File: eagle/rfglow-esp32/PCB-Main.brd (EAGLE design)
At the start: 20.1 x 75.9 mm, 27 parts, among them IC1 TLC59116PW, J1 4P-SMD-2.0-90D, J2 2P-2.0-90D-SMD, SW1 MK-12C02 G1.5, SW2 DHT-4235A, U1 XC6206P332MR-G-SOT23, U2 Value, X1 87438-06

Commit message: Consolidate libraries, swap regulator
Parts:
- removed C1: 100nf, Seeed-Capacitor:C0402
- ANT1: device Seeed-Connector:U-FL3P-SMD-2.6X2.6X1.0MM -> OPL_Connector:U-FL3P-SMD-2.6X2.6X1.0MM
- C2, C3: device Seeed-Capacitor:C0402 -> OPL_Capacitor:C0402
- J1: device Seeed-Connector:HW4-SMD-2.0-90D -> OPL_Connector:HW4-SMD-2.0-90D
- J2: device Seeed-Connector:HW2-SMD-2.0-90D -> OPL_Connector:HW2-SMD-2.0-90D
- R5, R6, R7: device Seeed-Resistor:R0402 -> OPL_Resistor:R0402
- R8, R9: value 10M 1/16W -> 1M; device Seeed-Resistor:R0402 -> OPL_Resistor:R0402
- SW1: device Seeed-Switch:SW7-SMD-L6.7X2.7X3.2MM -> OPL_Switch:SW7-SMD-L6.7X2.7X3.2MM
- SW2: device Seeed-Switch:SW4-SMD-4.2X3.2X2.5MM -> OPL_Switch:SW4-SMD-4.2X3.2X2.5MM
- U1: value XC6206P332MR-G-SOT23 -> AP2112K-3.3TRG1; device Seeed-IC:SOT-23 -> rfglow-esp32:SOT95P285X140-5N
- U2: device Webench-Regulator:DRC0010J -> Components:DRC0010J
- moved U1 71.2 mm to (-59.1, -16.6)
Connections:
- net GND: now also U1.2; no longer C1.1, U1.1
- net N$17: no longer C1.2
- net V3.3: now also U1.5; no longer U1.2
- net V4.2: now also U1.1

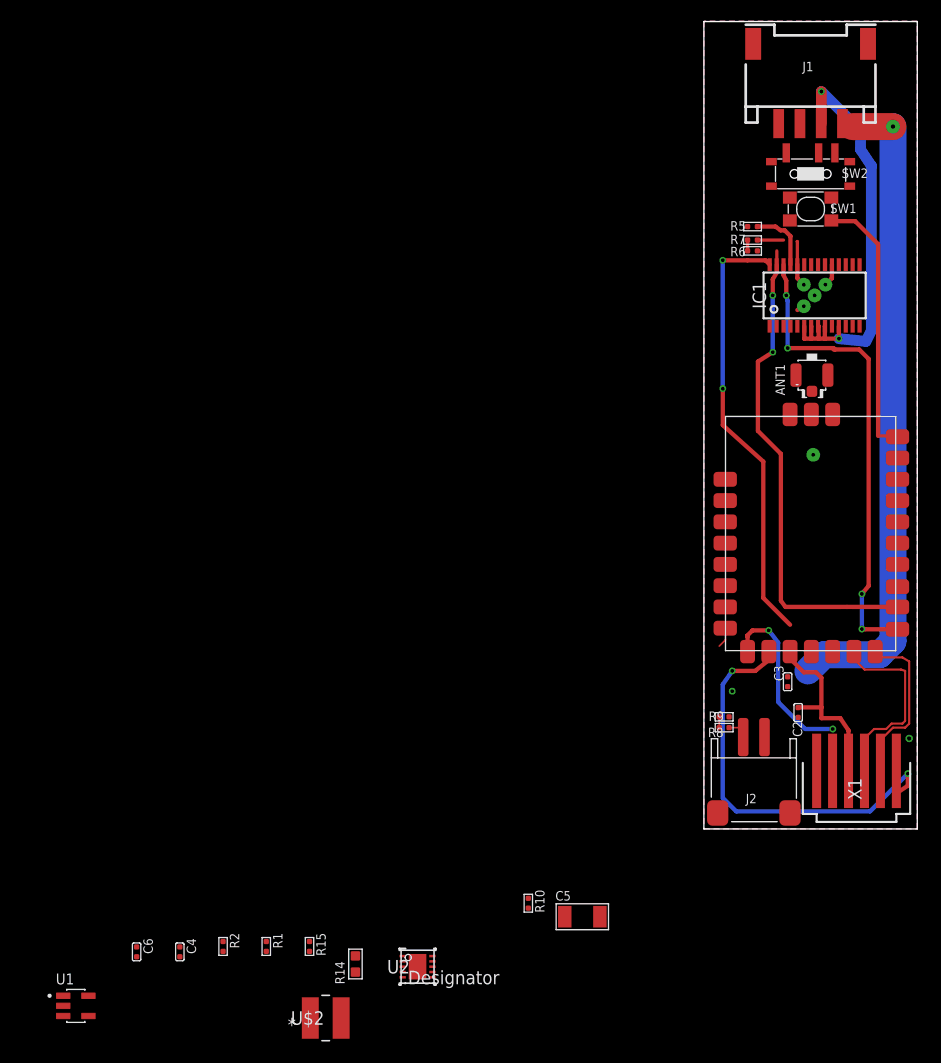
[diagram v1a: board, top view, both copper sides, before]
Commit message: Removed unused parts for esp32, begin integrating actual module
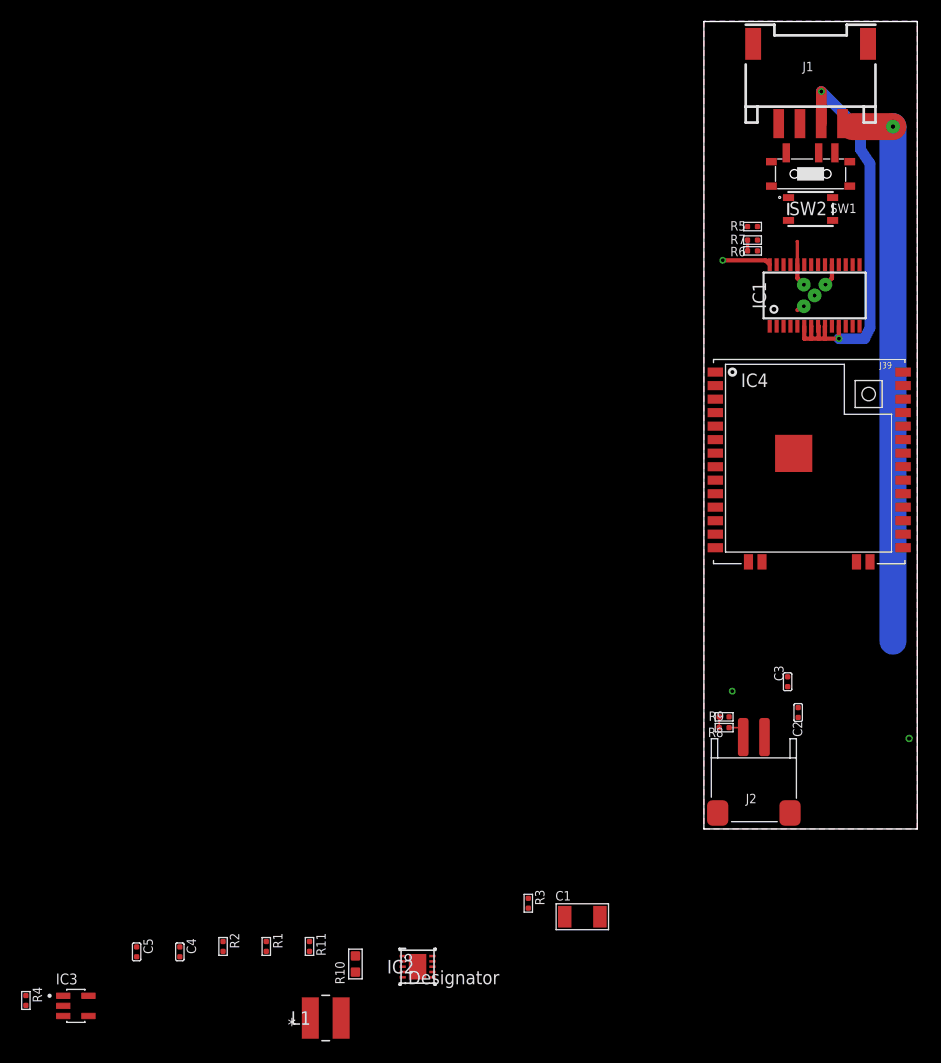
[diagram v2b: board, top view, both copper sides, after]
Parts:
- removed ANT1: U-FL, OPL_Connector:U-FL3P-SMD-2.6X2.6X1.0MM
- removed C6: 10uf, OPL_Capacitor:C0402
- removed R14: 56R, OPL_Resistor:R0603
- removed U$1: PANSTAMP-AVR-2, Components:SMD-PAD-34
- removed X1: 87438-06, Components:87438-06
- added C1: 100uf, OPL_Capacitor:C1206
- added IC4: ESP32-WROOM-32UNOSD, rfglow-esp32:XCVR_ESP32-WROOM-32U
- added R3: 1M, OPL_Resistor:R0402
- added R4: 100K, OPL_Resistor:R0402
- C5: value 100uf -> 10uf; device OPL_Capacitor:C1206 -> OPL_Capacitor:C0402
- R10: value 1M -> 56R; device OPL_Resistor:R0402 -> OPL_Resistor:R0603
- SW2: value DHT-4235A -> SKRPABE010; device OPL_Switch:SW4-SMD-4.2X3.2X2.5MM -> rfglow-esp32:SMT(4.2X3.2)
- moved C5 42.0 mm to (-53.3, -11.6)
- moved R10 17.2 mm to (-32.8, -12.7)
- renumbered R15 to R11, U$2 to L1, U1 to IC3, U2 to IC2
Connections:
- removed net ANT: ANT1.D, U$1.P$31
- removed net AREF: U$1.P$11, X1.2
- removed net N$17: R8.1, R9.2, U$1.P$10
- removed net RST: U$1.P$12, X1.6
- removed net RXD: U$1.P$17, X1.5
- removed net TXD: U$1.P$16, X1.4
- new net 3V3: IC4.2
- new net BATSENSE: R8.1, R9.2
- new net EXP: IC4.39
- new net N$4: IC3.3, R4.1
- net BUTTON: no longer U$1.P$27
- net GND: now also C1.1, IC4.1, IC4.15, IC4.38, R10.1; no longer ANT1.GND1, ANT1.GND2, C6.1, R14.1, U$1.P$14, U$1.P$30, U$1.P$32, X1.1
- net I2CSCL: no longer U$1.P$18
- net I2CSDA: no longer U$1.P$19
- net N$3: now also R3.1; no longer R10.1
- net N$5: now also R10.2; no longer R14.2
- net V3.3: no longer U$1.P$13, X1.3
- net V4.2: now also C1.2, R3.2, R4.2; no longer C5.2, IC3.3, R10.2
- net VBAT: now also C5.2; no longer C6.2
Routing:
- net V3.3: track 61.9 -> 5.59 mm, vias 2 -> 1
- net I2CSCL: track 47.5 -> 0.00 mm, vias 4 -> 0
- net I2CSDA: track 46.3 -> 0.00 mm, vias 2 -> 0
- net RST: track 42.0 -> 0.00 mm, vias 2 -> 0
- net BUTTON: track 25.2 -> 0.10 mm
- net RXD: track 19.6 -> 0.00 mm
- net AREF: track 17.0 -> 0.00 mm, vias 2 -> 0
- net TXD: track 15.6 -> 0.00 mm
- net V4.2: track 62.4 -> 53.3 mm
- net N$7: track 6.12 -> 0.00 mm
- net N$17: track 2.96 -> 0.00 mm
- net BATSENSE: track 0.00 -> 1.02 mm
- net GND: vias 7 -> 6

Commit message: Board layout with UART but without LIPO charger, submitted this one to PCBA
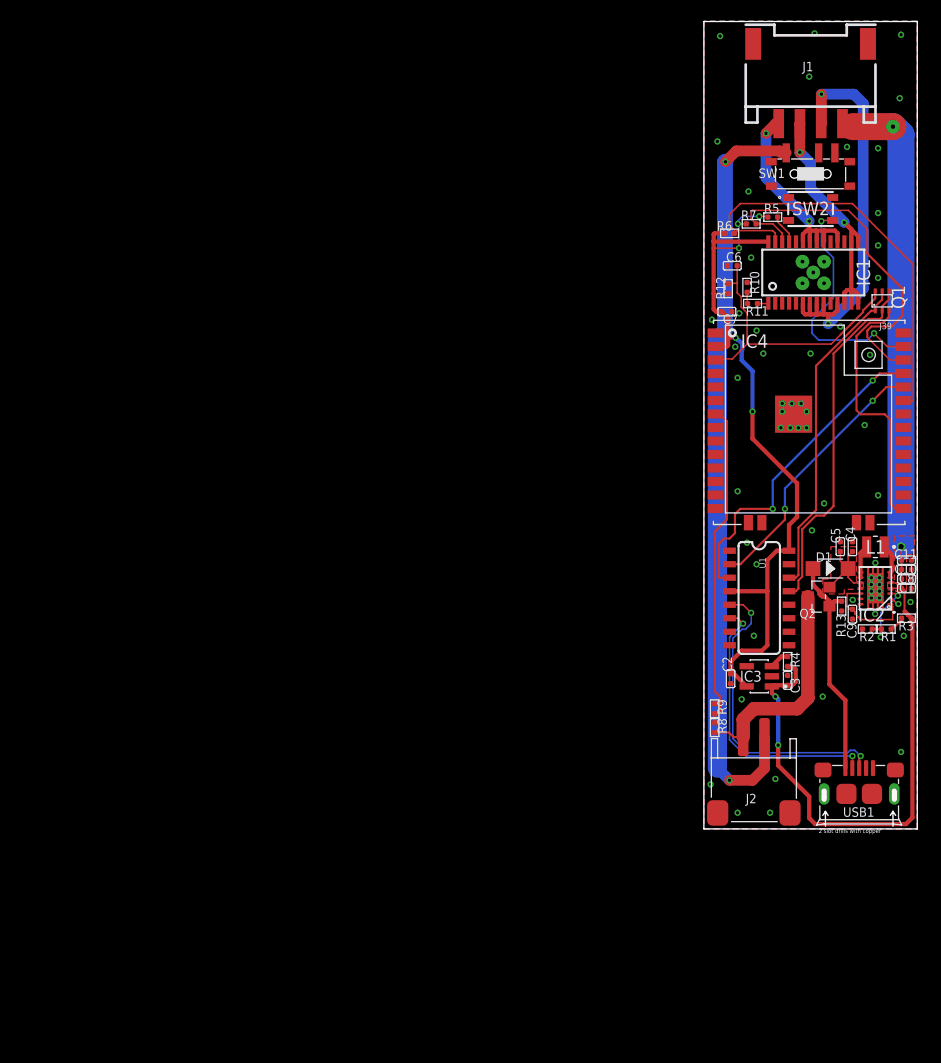
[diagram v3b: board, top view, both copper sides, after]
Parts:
- added C10, C11, C6, C7, C8: 10uf, OPL_Capacitor:C0402
- added C9: 100nf, OPL_Capacitor:C0402
- added D1: 20V-500MA, OPL_Discrete_Semiconductor:SOD-123
- added Q1: UMH3N, rfglow-esp32:UMT6
- added Q2: SSM3J328R,LF, OPL_Discrete_Semiconductor:SOT-23
- added R12: 10K 1/16W, OPL_Resistor:R0402
- added R13: 100K, OPL_Resistor:R0402
- added U1: CH340C, rfglow-esp32:SO016
- added USB1: 10118193-0001LF, OPL_Connector:MICRO-USB5+6P-SMD-0.65-B
- C1: value 100uf -> 10uf; device OPL_Capacitor:C1206 -> OPL_Capacitor:C0402
- IC1: device Components:PW_R-PDSO-G28 -> rfglow-esp32:PW_R-PDSO-G28
- IC2: value Value -> TPS63020; device Components:DRC0010J -> rfglow-esp32:QFN14-3X4MM
- IC4: value ESP32-WROOM-32UNOSD -> ESP32-WROOM-32U
- L1: value VLCF4020T-4R7N1R2 -> TFM252010ALM1R0MTAA; device Components:IND_4028 -> rfglow-esp32:IND_1008
- R10: device OPL_Resistor:R0603 -> rfglow-esp32:R0402
- R11, R3, R6, R7, R8, R9: device OPL_Resistor:R0402 -> rfglow-esp32:R0402
- moved R4 78.4 mm to (7.87, 15.7)
- moved C5 76.4 mm to (12.8, 26.5)
- moved C4 73.8 mm to (14.0, 26.5)
- moved R10 73.5 mm to (4.06, 50.9)
- moved R11 73.4 mm to (4.57, 49.4), turned to 90 degrees
- moved IC3 71.3 mm to (5.21, 14.4), turned to 180 degrees
- moved L1 68.1 mm to (16.1, 26.5), turned to 180 degrees
- moved R2 67.5 mm to (15.4, 18.8), turned to 90 degrees
- moved R1 65.5 mm to (17.1, 18.8), turned to 90 degrees
- moved IC2 55.9 mm to (16.1, 22.6), turned to 180 degrees
- moved R3 44.5 mm to (19.1, 19.8), turned to 90 degrees
- moved C1 43.4 mm to (19.1, 22.6), turned to 270 degrees
- moved C2 7.10 mm to (2.51, 14.1)
- moved IC4 3.68 mm to (9.90, 38.2)
- moved R6 2.72 mm to (2.41, 56.0)
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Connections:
- removed net 3V3: IC4.2
- removed net EXP: IC4.39
- new net D+: U1.5, USB1.3
- new net D-: U1.6, USB1.2
- new net DTR: Q1.2, Q1.4, U1.13
- new net GPIO0: IC4.25, Q1.3
- new net N$8: IC2.6, IC2.7, L1.1
- new net RESET: C6.1, IC4.3, Q1.6, R12.1
- new net RTS: Q1.1, Q1.5, U1.14
- new net RXD0: IC4.35, U1.3
- new net TXD0: IC4.34, U1.2
- new net VBUS: D1.+, Q2.1, R13.2, USB1.1
- new net VREGIN: C4.2, C5.2, D1.-, IC2.10, IC2.11, Q2.2
- net BATSENSE: now also IC4.7
- net BUTTON: now also IC4.37
- net GND: now also C10.1, C11.1, C6.2, C7.2, C8.1, C9.1, IC2.13, IC2.15, IC2.16, IC2.17, IC2.18, IC2.19, IC2.2, IC2.20, IC2.21, IC2.22, IC2.23, IC4.39, R13.1, U1.1, USB1.5, USB1.S1, USB1.S2, USB1.S3, USB1.S4, USB1.S5, USB1.S6; no longer IC2.11, IC2.3, IC2.9
- net I2CSCL: now also IC4.36
- net I2CSDA: now also IC4.33
- net N$1: now also C9.2, IC2.1, IC2.12; no longer IC2.4, L1.2
- net N$11: now also IC2.3; no longer IC2.10
- net N$6: now also IC2.8, IC2.9, L1.2; no longer IC2.2, L1.1
- net V3.3: now also C7.1, IC4.2, R12.2, U1.16, U1.4
- net V4.2: now also C10.2, C11.2, C8.2, IC2.4, IC2.5; no longer IC2.1
- net VBAT: now also Q2.3; no longer C4.2, C5.2, IC2.5, IC2.6, IC2.7, IC2.8
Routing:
- net BAT-: track 0.00 -> 71.9 mm, vias 0 -> 2
- net V3.3: track 5.59 -> 73.7 mm, vias 1 -> 5
- net V4.2: track 53.3 -> 101.4 mm, vias 1 -> 4
- net I2CSDA: track 0.00 -> 40.8 mm
- net I2CSCL: track 0.00 -> 34.9 mm
- net DTR: track 0.00 -> 33.6 mm
- net RTS: track 0.00 -> 31.2 mm
- net RXD0: track 0.00 -> 30.8 mm, vias 0 -> 2
- net BATSENSE: track 1.02 -> 30.9 mm
- net D+: track 0.00 -> 29.1 mm, vias 0 -> 2
- net RESET: track 0.00 -> 26.9 mm
- net D-: track 0.00 -> 26.3 mm, vias 0 -> 2
- net TXD0: track 0.00 -> 24.9 mm, vias 0 -> 2
- net GREEN-: track 0.00 -> 24.7 mm, vias 0 -> 2
- net GPIO0: track 0.00 -> 24.2 mm
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- added copper zone on layer 1, net V4.2
- added copper zone on layer 1, net VREGIN
